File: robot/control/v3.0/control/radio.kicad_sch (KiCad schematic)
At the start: 1 part, among them J1 BM10B-SRSS-TB

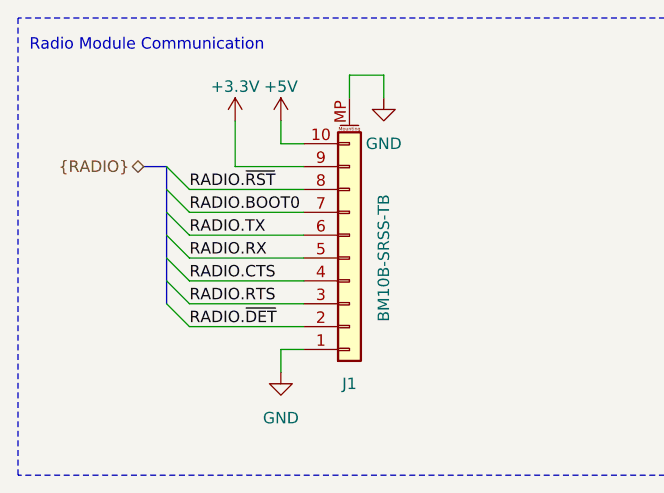
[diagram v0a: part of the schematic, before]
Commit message: control v3 passing ERC
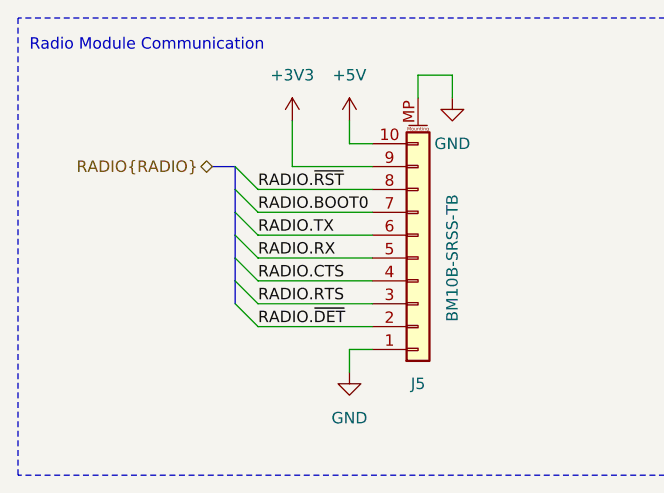
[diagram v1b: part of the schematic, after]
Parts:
- renumbered J1 to J5
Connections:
- net +3.3V renamed +3V3
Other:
- moved on the sheet: J5

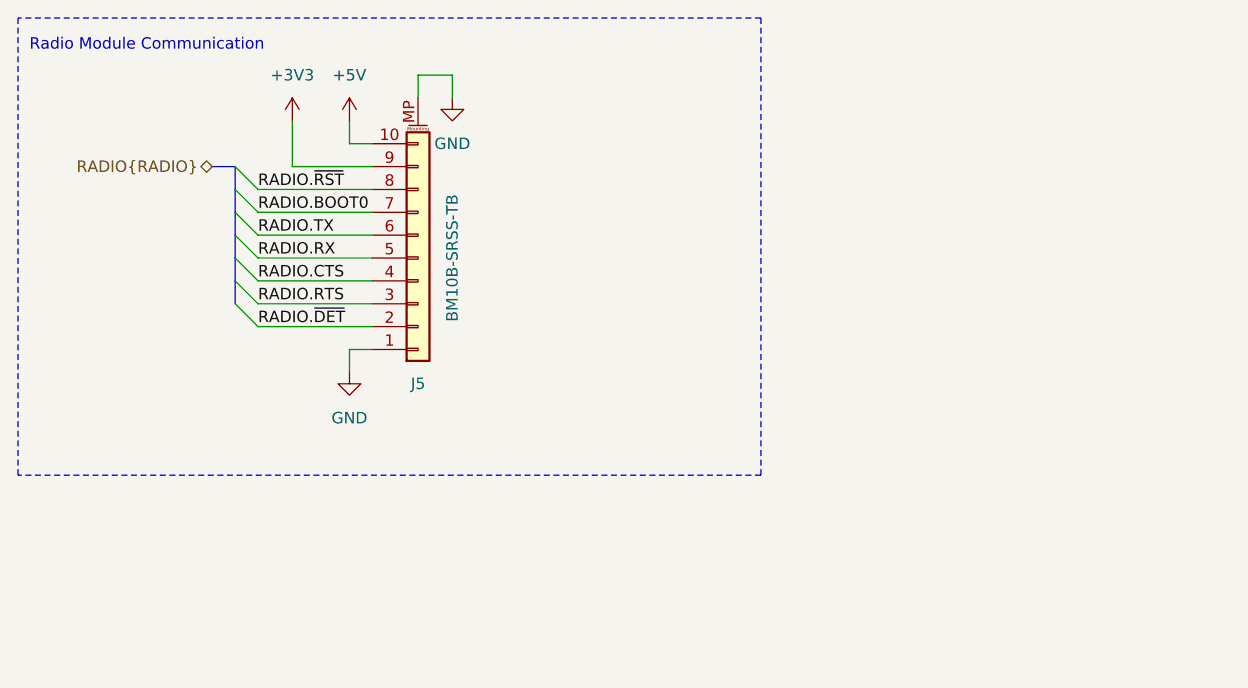
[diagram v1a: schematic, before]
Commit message: update boot mode docs, schematic visual fixes, UART default state fixes
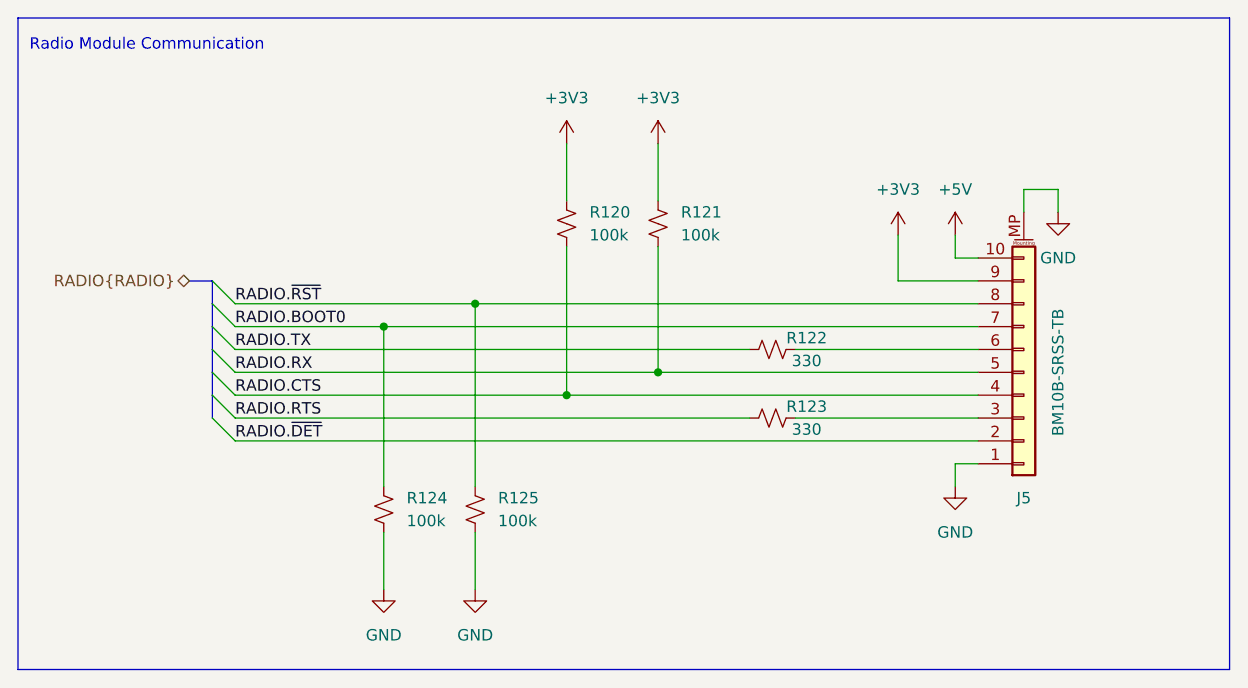
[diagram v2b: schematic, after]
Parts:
- added R120, R121, R124, R125: 100k, Resistor_SMD:R_0402_1005Metric, symbol Device:R_Small_US
- added R122, R123: 330, Resistor_SMD:R_0402_1005Metric, symbol Device:R_Small_US
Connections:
- net +3V3: now also R120.1, R121.1
- net GND: now also R124.2, R125.2
- net RADIO.BOOT0: now also R124.1
- net RADIO.CTS: now also R120.2
- net RADIO.RTS: now also R123.1; no longer J5.3 (Pin_3)
- net RADIO.RX: now also R121.2
- net RADIO.TX: now also R122.1; no longer J5.6 (Pin_6)
- net RADIO.~{RST}: now also R125.1
- new net: J5.3 (Pin_3), R123.2
- new net: J5.6 (Pin_6), R122.2
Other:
- moved on the sheet: J5
